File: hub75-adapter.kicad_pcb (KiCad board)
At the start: 2 copper layers, 21.8 x 64.6 mm, 9 parts, among them J1 PI, J2 5V_IN, J3 HUB75, J4 5V_OUT_MATRIX

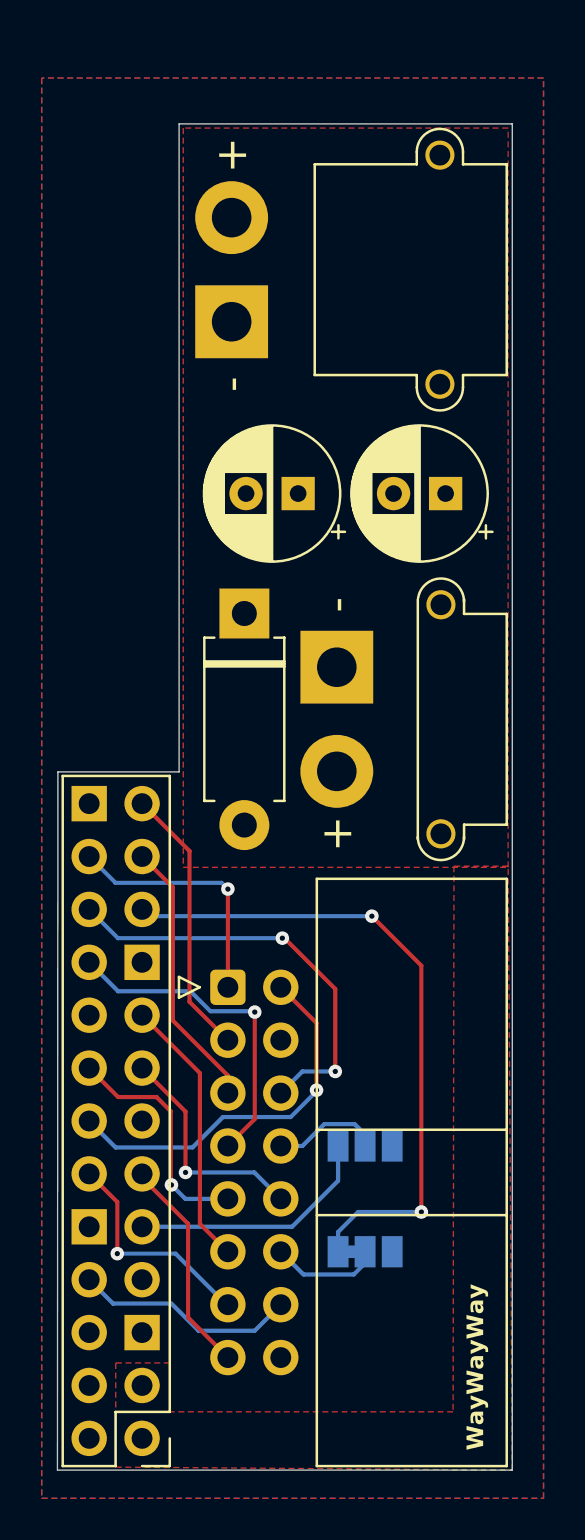
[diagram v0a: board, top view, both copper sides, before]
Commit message: rev2 w/ oe resistor
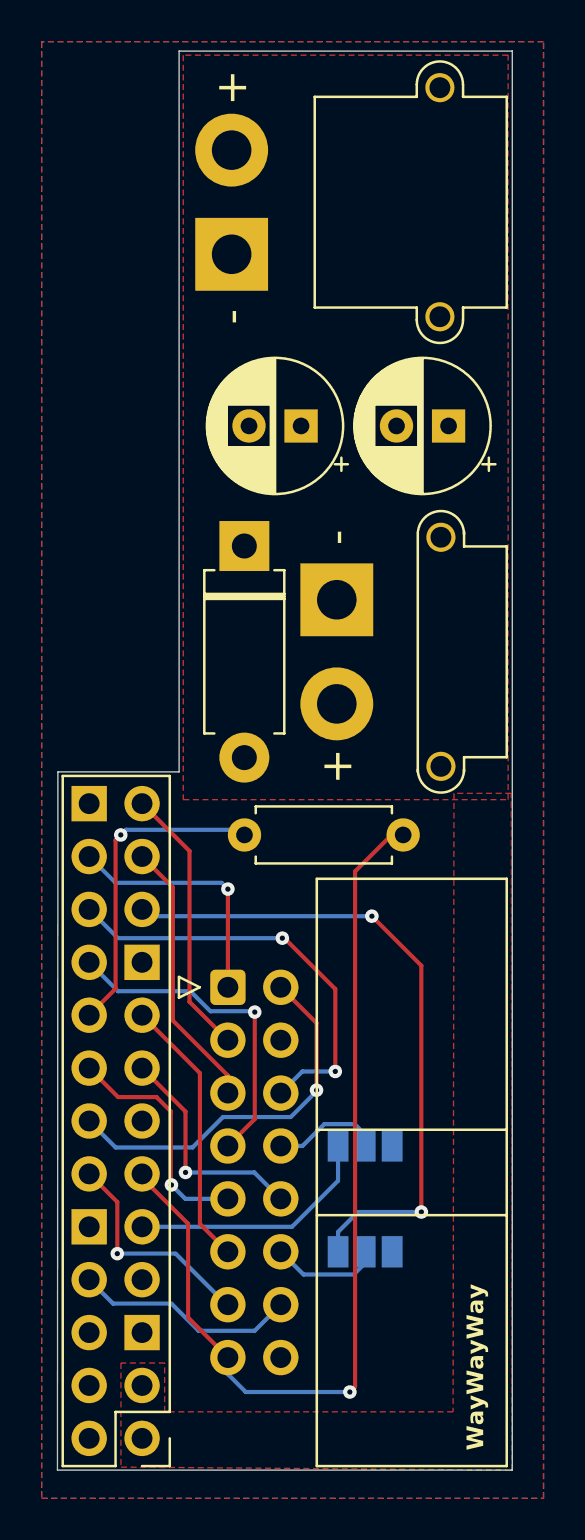
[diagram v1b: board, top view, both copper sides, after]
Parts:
- added R1: 10k, Resistor_THT:R_Axial_DIN0207_L6.3mm_D2.5mm_P7.62mm_Horizontal, F.Cu at (13.8, 3.03)
- moved C2 3.25 mm to (16.0, -16.6)
- moved C3 3.25 mm to (8.89, -16.6)
- moved J2 3.24 mm to (5.56, -24.9)
- moved D1 3.24 mm to (6.17, -10.8)
- moved J4 3.24 mm to (10.6, -8.27)
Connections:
- J1 pad 1: unconnected-(J1-3V3-Pad1) -> +3V3
- J1 pad 17: unconnected-(J1-3V3-Pad1)_1 -> +3V3
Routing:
- net /~{OE}: track 10.5 -> 45.7 mm, vias 0 -> 1
- net +3V3: track 0.00 -> 15.4 mm, vias 0 -> 1
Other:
- board size 21.8 x 64.6 mm -> 21.8 x 68.1 mm
- board text added: "pi2hub75 v2 @knifa"
- board text removed: "pi2hub75 v1 @knifa"
